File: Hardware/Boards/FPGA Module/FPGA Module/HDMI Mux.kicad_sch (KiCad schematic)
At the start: 3 parts, among them U14 TS3USB221A

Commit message: FPGA Module sch update
Added 3V3 LDO for MCU and 3V3 EN for DCDC. Also added SPI bus from MCU to FPGA with level shifter
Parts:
- added R129: 4.7K, Resistor_SMD:R_0402_1005Metric, symbol Device:R_US
- added TP45: Test Point, FPGA Module:Test Point 0.75mm, symbol Connector:TestPoint
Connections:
- net GND: now also R129.1; no longer U14.6 (~{EN})
- net HDMI_CLK_SEL: now also TP45.1
- new net: R129.2, U14.6 (~{EN})
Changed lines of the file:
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@@
 		(color 0 0 0 0)
 	)
+	(junction
+		(at 179.07 152.4)
+		(diameter 0)
+		(color 0 0 0 0)
+	)
 	(wire
 		(pts
@@
 	(wire
 		(pts
+			(xy 198.12 166.37) (xy 198.12 167.64)
+		)
+		(stroke
+			(width 0)
+			(type default)
+		)
+	)
+	(wire
+		(pts
 			(xy 218.44 128.27) (xy 218.44 129.54)
 		)
@@
 	(wire
 		(pts
+			(xy 179.07 152.4) (xy 185.42 152.4)
+		)
+		(stroke
+			(width 0)
+			(type default)
+		)
+	)
+	(wire
+		(pts
 			(xy 185.42 152.4) (xy 199.39 152.4)
 		)
@@
 	(wire
 		(pts
-			(xy 181.61 152.4) (xy 185.42 152.4)
-		)
-		(stroke
-			(width 0)
-			(type default)
-		)
-	)
-	(wire
-		(pts
-			(xy 198.12 154.94) (xy 198.12 162.56)
+			(xy 175.26 152.4) (xy 179.07 152.4)
+		)
+		(stroke
+			(width 0)
+			(type default)
+		)
+	)
+	(wire
+		(pts
+			(xy 198.12 154.94) (xy 198.12 158.75)
 		)
 		(stroke
@@
 	(hierarchical_label "HDMI_CLK_SEL"
 		(shape input)
-		(at 181.61 152.4 180)
+		(at 175.26 152.4 180)
 		(fields_autoplaced yes)
 		(effects
@@
 	)
 	(symbol
+		(lib_id "Device:R_US")
+		(at 198.12 162.56 180)
+		(unit 1)
+		(exclude_from_sim no)
+		(in_bom yes)
+		(on_board yes)
+		(dnp no)
+		(property "Reference" "R129"
+			(at 200.66 161.2899 0)
+			(effects
+				(font
+					(size 1.27 1.27)
+				)
+				(justify right)
+			)
+		)
+		(property "Value" "4.7K"
+			(at 200.66 163.8299 0)
+			(effects
+				(font
+					(size 1.27 1.27)
+				)
+				(justify right)
+			)
+		)
+		(property "Footprint" "Resistor_SMD:R_0402_1005Metric"
+			(at 197.104 162.306 90)
+			(effects
+				(font
+					(size 1.27 1.27)
+				)
+				(hide yes)
+			)
+		)
+		(property "Datasheet" "~"
+			(at 198.12 162.56 0)
+			(effects
+				(font
+					(size 1.27 1.27)
+				)
+				(hide yes)
+			)
+		)
+		(property "Description" "Resistor, US symbol"
+			(at 198.12 162.56 0)
+			(effects
+				(font
+					(size 1.27 1.27)
+				)
+				(hide yes)
+			)
+		)
+		(pin "1"
+		)
+		(pin "2"
+		)
+		(instances
+			(project "FPGA Module"
+				(path "/199f10e2-d4b4-4a27-9e84-7b1ce2ae6bf0/0c296310-f788-47f0-8a3f-43c3444563e8/e6896036-c481-4794-bc56-64749c97c534"
+					(reference "R129")
+					(unit 1)
+				)
+			)
+		)
+	)
+	(symbol
 		(lib_id "FPGA Module:TS3USB221A")
 		(at 214.63 129.54 0)
@@
 	(symbol
 		(lib_id "power:GND")
-		(at 198.12 162.56 0)
-		(unit 1)
-		(exclude_from_sim no)
-		(in_bom yes)
-		(on_board yes)
-		(dnp no)
-		(property "Reference" "#PWR0268"
-			(at 198.12 168.91 0)
-			(effects
-				(font
-					(size 1.27 1.27)
-				)
-				(hide yes)
-			)
-		)
-		(property "Value" "GND"
-			(at 198.12 166.37 0)
-			(effects
-				(font
-					(size 1.27 1.27)
-				)
-			)
-		)
-		(property "Footprint" ""
-			(at 198.12 162.56 0)
-			(effects
-				(font
-					(size 1.27 1.27)
-				)
-				(hide yes)
-			)
-		)
-		(property "Datasheet" ""
-			(at 198.12 162.56 0)
-			(effects
-				(font
-					(size 1.27 1.27)
-				)
-				(hide yes)
-			)
-		)
-		(property "Description" "Power symbol creates a global label with name \"GND\" , ground"
-			(at 198.12 162.56 0)
-			(effects
-				(font
-					(size 1.27 1.27)
-				)
-				(hide yes)
-			)
-		)
-		(pin "1"
-		)
-		(instances
-			(project "FPGA Module"
-				(path "/199f10e2-d4b4-4a27-9e84-7b1ce2ae6bf0/0c296310-f788-47f0-8a3f-43c3444563e8/e6896036-c481-4794-bc56-64749c97c534"
-					(reference "#PWR0268")
-					(unit 1)
-				)
-			)
-		)
-	)
-	(symbol
-		(lib_id "power:GND")
 		(at 218.44 134.62 0)
 		(unit 1)
@@
 					(unit 1)
 				)
+			)
+		)
+	)
+	(symbol
+		(lib_id "Connector:TestPoint")
+		(at 179.07 152.4 0)
+		(unit 1)
+		(exclude_from_sim no)
+		(in_bom yes)
+		(on_board yes)
+		(dnp no)
+		(property "Reference" "TP45"
+			(at 176.53 147.32 0)
+			(effects
+				(font
+					(size 1.27 1.27)
+				)
+				(justify left)
+			)
+		)
+		(property "Value" "Test Point"
+			(at 173.99 146.685 0)
+			(effects
+				(font
+					(size 1.27 1.27)
+				)
+				(justify left)
+				(hide yes)
+			)
+		)
+		(property "Footprint" "FPGA Module:Test Point 0.75mm"
+			(at 184.15 152.4 0)
+			(effects
+				(font
+					(size 1.27 1.27)
+				)
+				(hide yes)
+			)
+		)
+		(property "Datasheet" "~"
+			(at 184.15 152.4 0)
+			(effects
+				(font
+					(size 1.27 1.27)
+				)
+				(hide yes)
+			)
+		)
+		(property "Description" "test point"
+			(at 179.07 152.4 0)
+			(effects
+				(font
+					(size 1.27 1.27)
+				)
+				(hide yes)
+			)
+		)
+		(pin "1"
+		)
+		(instances
+			(project "FPGA Module"
+				(path "/199f10e2-d4b4-4a27-9e84-7b1ce2ae6bf0/0c296310-f788-47f0-8a3f-43c3444563e8/e6896036-c481-4794-bc56-64749c97c534"
+					(reference "TP45")
+					(unit 1)
+				)
+			)
+		)
+	)
+	(symbol
+		(lib_id "power:GND")
+		(at 198.12 167.64 0)
+		(unit 1)
+		(exclude_from_sim no)
+		(in_bom yes)
+		(on_board yes)
+		(dnp no)
+		(property "Reference" "#PWR0268"
+			(at 198.12 173.99 0)
+			(effects
+				(font
+					(size 1.27 1.27)
+				)
+				(hide yes)
+			)
+		)
+		(property "Value" "GND"
+			(at 198.12 171.45 0)
+			(effects
+				(font
+					(size 1.27 1.27)
+				)
+			)
+		)
+		(property "Footprint" ""
+			(at 198.12 167.64 0)
+			(effects
+				(font
+					(size 1.27 1.27)
+				)
+				(hide yes)
+			)
+		)
+		(property "Datasheet" ""
+			(at 198.12 167.64 0)
+			(effects
+				(font
+					(size 1.27 1.27)
+				)
+				(hide yes)
+			)
+		)
+		(property "Description" "Power symbol creates a global label with name \"GND\" , ground"
+			(at 198.12 167.64 0)
+			(effects
+				(font
+					(size 1.27 1.27)
+				)
+				(hide yes)
+			)
+		)
+		(pin "1"
+		)
+		(instances
+			(project "FPGA Module"
+				(path "/199f10e2-d4b4-4a27-9e84-7b1ce2ae6bf0/0c296310-f788-47f0-8a3f-43c3444563e8/e6896036-c481-4794-bc56-64749c97c534"
+					(reference "#PWR0268")
+					(unit 1)
+				)

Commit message: Completed FPGA module PCB layout
Started PCB routing
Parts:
- C125: renamed from C136; footprint Capacitor_SMD:C_0402_1005Metric -> Capacitor_SMD:C_0201_0603Metric
- R127: renamed from R109; footprint Resistor_SMD:R_0402_1005Metric -> Resistor_SMD:R_0201_0603Metric
- R128: renamed from R129; footprint Resistor_SMD:R_0402_1005Metric -> Resistor_SMD:R_0201_0603Metric
- renumbered TP45 to TP52, U14 to U22
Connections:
- net HDMI_GTCLK_N: now also U22.2 (D1-); no longer U22.4 (D2-)
- net HDMI_GTCLK_P: now also U22.1 (D1+); no longer U22.3 (D2+)
- net HDMI_LVCLK_N: now also U22.4 (D2-); no longer U22.2 (D1-)
- net HDMI_LVCLK_P: now also U22.3 (D2+); no longer U22.1 (D1+)
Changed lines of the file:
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@@
+	(wire
+		(pts
+			(xy 175.26 144.78) (xy 199.39 144.78)
+		)
+		(stroke
+			(width 0)
+			(type default)
+		)
+	)
 	(wire
 		(pts
@@
 	(wire
 		(pts
+			(xy 175.26 129.54) (xy 199.39 129.54)
+		)
+		(stroke
+			(width 0)
+			(type default)
+		)
+	)
+	(wire
+		(pts
 			(xy 198.12 166.37) (xy 198.12 167.64)
 		)
@@
 	(wire
 		(pts
+			(xy 175.26 142.24) (xy 199.39 142.24)
+		)
+		(stroke
+			(width 0)
+			(type default)
+		)
+	)
+	(wire
+		(pts
 			(xy 218.44 128.27) (xy 218.44 129.54)
 		)
@@
 	(wire
 		(pts
-			(xy 175.26 129.54) (xy 199.39 129.54)
-		)
-		(stroke
-			(width 0)
-			(type default)
-		)
-	)
-	(wire
-		(pts
 			(xy 217.17 144.78) (xy 233.68 144.78)
 		)
@@
 	(wire
 		(pts
-			(xy 175.26 142.24) (xy 199.39 142.24)
-		)
-		(stroke
-			(width 0)
-			(type default)
-		)
-	)
-	(wire
-		(pts
-			(xy 175.26 144.78) (xy 199.39 144.78)
-		)
-		(stroke
-			(width 0)
-			(type default)
-		)
-	)
-	(wire
-		(pts
 			(xy 175.26 152.4) (xy 179.07 152.4)
 		)
@@
 		)
 	)
-	(text_box "NOTE: Default is Output ON, HDMI_CLK <- LVDS IO\nPull Sel HIGH to connect HDMI_CLK to MGT IO"
+	(text_box "NOTE: Default is Output ON, HDMI_CLK <- MGT IO\nPull Sel HIGH to connect HDMI_CLK to LVDS IO"
 		(exclude_from_sim no)
 		(at 150.495 155.575 0)
@@
 		)
 	)
+	(label "HDMI_GTCLK_P"
+		(at 175.26 129.54 0)
+		(fields_autoplaced yes)
+		(effects
+			(font
+				(size 1.27 1.27)
+			)
+			(justify left bottom)
+		)
+	)
 	(label "HDMI_CLK_SEL"
 		(at 181.61 152.4 0)
@@
 		)
 	)
+	(label "HDMI_GTCLK_N"
+		(at 175.26 132.08 0)
+		(fields_autoplaced yes)
+		(effects
+			(font
+				(size 1.27 1.27)
+			)
+			(justify left bottom)
+		)
+	)
+	(label "HDMI_LVCLK_P"
+		(at 175.26 142.24 0)
+		(fields_autoplaced yes)
+		(effects
+			(font
+				(size 1.27 1.27)
+			)
+			(justify left bottom)
+		)
+	)
 	(label "HDMI_LVCLK_N"
-		(at 175.26 132.08 0)
-		(fields_autoplaced yes)
-		(effects
-			(font
-				(size 1.27 1.27)
-			)
-			(justify left bottom)
-		)
-	)
-	(label "HDMI_GTCLK_P"
-		(at 175.26 142.24 0)
-		(fields_autoplaced yes)
-		(effects
-			(font
-				(size 1.27 1.27)
-			)
-			(justify left bottom)
-		)
-	)
-	(label "HDMI_GTCLK_N"
 		(at 175.26 144.78 0)
 		(fields_autoplaced yes)
@@
 		)
 	)
-	(label "HDMI_LVCLK_P"
-		(at 175.26 129.54 0)
-		(fields_autoplaced yes)
-		(effects
-			(font
-				(size 1.27 1.27)
-			)
-			(justify left bottom)
-		)
-	)
 	(label "HDMI_CLK_N"
 		(at 233.68 144.78 180)
@@
 	(hierarchical_label "HDMI_LVCLK_N"
 		(shape input)
-		(at 175.26 132.08 180)
+		(at 175.26 144.78 180)
 		(fields_autoplaced yes)
 		(effects
@@
 		)
 	)
-	(hierarchical_label "HDMI_GTCLK_P"
+	(hierarchical_label "HDMI_LVCLK_P"
 		(shape input)
 		(at 175.26 142.24 180)
-		(fields_autoplaced yes)
-		(effects
-			(font
-				(size 1.27 1.27)
-			)
-			(justify right)
-		)
-	)
-	(hierarchical_label "HDMI_LVCLK_P"
-		(shape input)
-		(at 175.26 129.54 180)
-		(fields_autoplaced yes)
-		(effects
-			(font
-				(size 1.27 1.27)
-			)
-			(justify right)
-		)
-	)
-	(hierarchical_label "HDMI_GTCLK_N"
-		(shape input)
-		(at 175.26 144.78 180)
 		(fields_autoplaced yes)
 		(effects
@@
 			)
 			(justify left)
+		)
+	)
+	(hierarchical_label "HDMI_GTCLK_P"
+		(shape input)
+		(at 175.26 129.54 180)
+		(fields_autoplaced yes)
+		(effects
+			(font
+				(size 1.27 1.27)
+			)
+			(justify right)
+		)
+	)
+	(hierarchical_label "HDMI_GTCLK_N"
+		(shape input)
+		(at 175.26 132.08 180)
+		(fields_autoplaced yes)
+		(effects
+			(font
+				(size 1.27 1.27)
+			)
+			(justify right)
 		)
 	)
@@
 		(on_board yes)
 		(dnp no)
-		(property "Reference" "R109"
+		(property "Reference" "R127"
 			(at 187.96 156.2099 0)
 			(effects
@@
 			)
 		)
-		(property "Footprint" "Resistor_SMD:R_0402_1005Metric"
+		(property "Footprint" "Resistor_SMD:R_0201_0603Metric"
 			(at 184.404 157.226 90)
 			(effects
@@
 			(project "FPGA Module"
 				(path "/199f10e2-d4b4-4a27-9e84-7b1ce2ae6bf0/0c296310-f788-47f0-8a3f-43c3444563e8/e6896036-c481-4794-bc56-64749c97c534"
-					(reference "R109")
+					(reference "R127")
 					(unit 1)
 				)
@@
 		(on_board yes)
 		(dnp no)
-		(property "Reference" "C136"
+		(property "Reference" "C125"
 			(at 220.98 130.8162 0)
 			(effects
@@
 			)
 		)
-		(property "Footprint" "Capacitor_SMD:C_0402_1005Metric"
+		(property "Footprint" "Capacitor_SMD:C_0201_0603Metric"
 			(at 218.44 132.08 0)
 			(effects
@@
 			(project "FPGA Module"
 				(path "/199f10e2-d4b4-4a27-9e84-7b1ce2ae6bf0/0c296310-f788-47f0-8a3f-43c3444563e8/e6896036-c481-4794-bc56-64749c97c534"
-					(reference "C136")
+					(reference "C125")
 					(unit 1)
 				)
@@
 		(on_board yes)
 		(dnp no)
-		(property "Reference" "#PWR0267"
+		(property "Reference" "#PWR0276"
 			(at 218.44 168.91 0)
 			(effects
@@
 			(project "FPGA Module"
 				(path "/199f10e2-d4b4-4a27-9e84-7b1ce2ae6bf0/0c296310-f788-47f0-8a3f-43c3444563e8/e6896036-c481-4794-bc56-64749c97c534"
-					(reference "#PWR0267")
+					(reference "#PWR0276")
 					(unit 1)
 				)
@@
 		(on_board yes)
 		(dnp no)
-		(property "Reference" "R129"
+		(property "Reference" "R128"
 			(at 200.66 161.2899 0)
 			(effects
@@
 			)
 		)
-		(property "Footprint" "Resistor_SMD:R_0402_1005Metric"
+		(property "Footprint" "Resistor_SMD:R_0201_0603Metric"
 			(at 197.104 162.306 90)
 			(effects
@@
 			(project "FPGA Module"
 				(path "/199f10e2-d4b4-4a27-9e84-7b1ce2ae6bf0/0c296310-f788-47f0-8a3f-43c3444563e8/e6896036-c481-4794-bc56-64749c97c534"
-					(reference "R129")
+					(reference "R128")
 					(unit 1)
 				)
@@
 		(dnp no)
 		(fields_autoplaced yes)
-		(property "Reference" "U14"
+		(property "Reference" "U22"
 			(at 208.28 121.92 0)
 			(effects
@@
 			(project ""
 				(path "/199f10e2-d4b4-4a27-9e84-7b1ce2ae6bf0/0c296310-f788-47f0-8a3f-43c3444563e8/e6896036-c481-4794-bc56-64749c97c534"
-					(reference "U14")
+					(reference "U22")
 					(unit 1)
 				)
@@
 		(on_board yes)
 		(dnp no)
-		(property "Reference" "#PWR0269"
+		(property "Reference" "#PWR0275"
 			(at 185.42 168.91 0)
 			(effects
@@
 			(project "FPGA Module"
 				(path "/199f10e2-d4b4-4a27-9e84-7b1ce2ae6bf0/0c296310-f788-47f0-8a3f-43c3444563e8/e6896036-c481-4794-bc56-64749c97c534"
-					(reference "#PWR0269")
+					(reference "#PWR0275")
 					(unit 1)
 				)
@@
 		(on_board yes)
 		(dnp no)
-		(property "Reference" "#PWR0265"
+		(property "Reference" "#PWR0274"
 			(at 218.44 140.97 0)
 			(effects
@@
 			(project "FPGA Module"
 				(path "/199f10e2-d4b4-4a27-9e84-7b1ce2ae6bf0/0c296310-f788-47f0-8a3f-43c3444563e8/e6896036-c481-4794-bc56-64749c97c534"
-					(reference "#PWR0265")
+					(reference "#PWR0274")
 					(unit 1)
 				)
@@
 		(on_board yes)
 		(dnp no)
-		(property "Reference" "TP45"
+		(property "Reference" "TP52"
 			(at 176.53 147.32 0)
 			(effects
@@
 			(project "FPGA Module"
 				(path "/199f10e2-d4b4-4a27-9e84-7b1ce2ae6bf0/0c296310-f788-47f0-8a3f-43c3444563e8/e6896036-c481-4794-bc56-64749c97c534"
-					(reference "TP45")
+					(reference "TP52")
 					(unit 1)
 				)
@@
 		(on_board yes)
 		(dnp no)
-		(property "Reference" "#PWR0268"
+		(property "Reference" "#PWR0277"
 			(at 198.12 173.99 0)
 			(effects
@@
 			(project "FPGA Module"
 				(path "/199f10e2-d4b4-4a27-9e84-7b1ce2ae6bf0/0c296310-f788-47f0-8a3f-43c3444563e8/e6896036-c481-4794-bc56-64749c97c534"
-					(reference "#PWR0268")
+					(reference "#PWR0277")
 					(unit 1)
 				)
@@
 		(on_board yes)
 		(dnp no)
-		(property "Reference" "#PWR0266"
+		(property "Reference" "#PWR0273"
 			(at 218.44 132.08 0)
 			(effects
@@
 			(project "FPGA Module"
 				(path "/199f10e2-d4b4-4a27-9e84-7b1ce2ae6bf0/0c296310-f788-47f0-8a3f-43c3444563e8/e6896036-c481-4794-bc56-64749c97c534"
-					(reference "#PWR0266")
+					(reference "#PWR0273")
 					(unit 1)
 				)

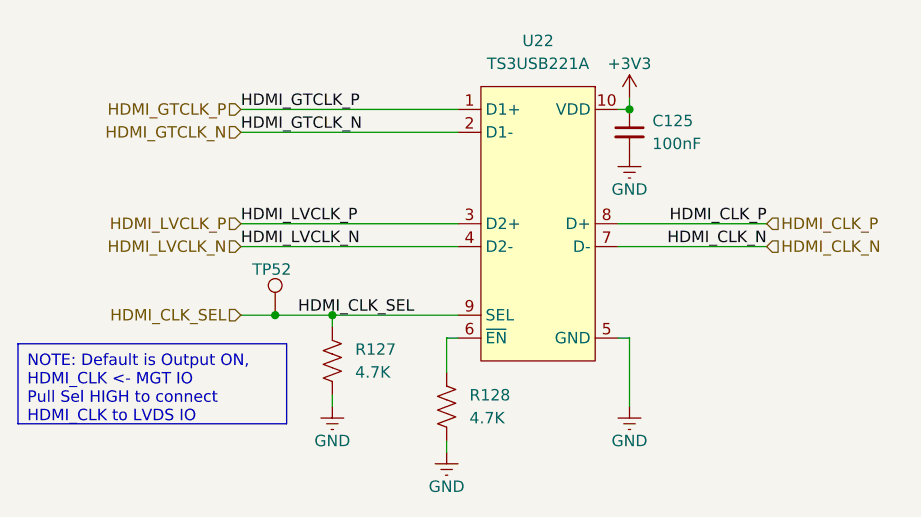
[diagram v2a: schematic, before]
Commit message: Fixed FPGA Module Routing
Reversed B2B headers and re-routed connections to FPGA
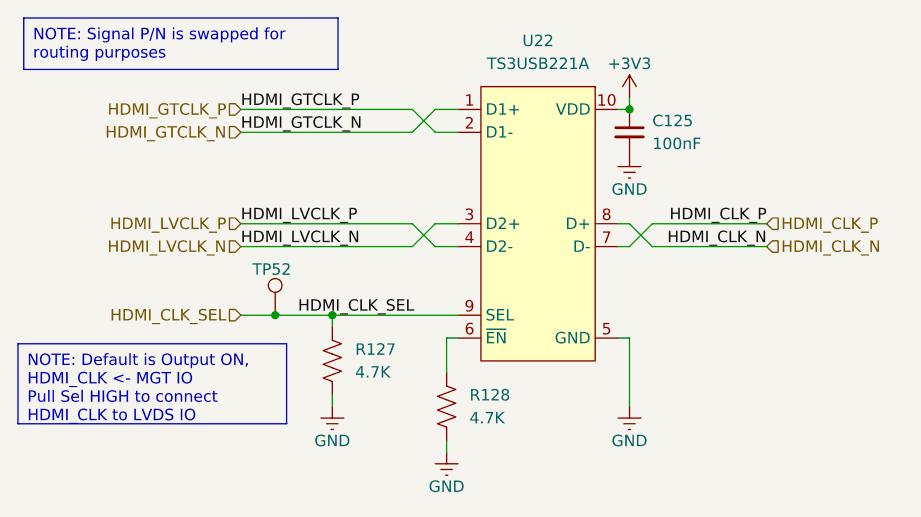
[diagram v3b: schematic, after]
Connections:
- net HDMI_CLK_N: now also U22.8 (D+); no longer U22.7 (D-)
- net HDMI_CLK_P: now also U22.7 (D-); no longer U22.8 (D+)
- net HDMI_GTCLK_N: now also U22.1 (D1+); no longer U22.2 (D1-)
- net HDMI_GTCLK_P: now also U22.2 (D1-); no longer U22.1 (D1+)
- net HDMI_LVCLK_N: now also U22.3 (D2+); no longer U22.4 (D2-)
- net HDMI_LVCLK_P: now also U22.4 (D2-); no longer U22.3 (D2+)
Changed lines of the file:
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@@
 	(wire
 		(pts
-			(xy 175.26 144.78) (xy 199.39 144.78)
+			(xy 217.17 142.24) (xy 218.44 142.24)
+		)
+		(stroke
+			(width 0)
+			(type default)
+		)
+	)
+	(wire
+		(pts
+			(xy 194.31 132.08) (xy 196.85 129.54)
 		)
 		(stroke
@@
 	(wire
 		(pts
-			(xy 175.26 129.54) (xy 199.39 129.54)
-		)
-		(stroke
-			(width 0)
-			(type default)
-		)
-	)
-	(wire
-		(pts
 			(xy 198.12 166.37) (xy 198.12 167.64)
 		)
@@
 	(wire
 		(pts
-			(xy 175.26 142.24) (xy 199.39 142.24)
-		)
-		(stroke
-			(width 0)
-			(type default)
-		)
-	)
-	(wire
-		(pts
 			(xy 218.44 128.27) (xy 218.44 129.54)
 		)
@@
 	(wire
 		(pts
+			(xy 196.85 142.24) (xy 199.39 142.24)
+		)
+		(stroke
+			(width 0)
+			(type default)
+		)
+	)
+	(wire
+		(pts
 			(xy 199.39 154.94) (xy 198.12 154.94)
 		)
@@
 	(wire
 		(pts
+			(xy 194.31 144.78) (xy 196.85 142.24)
+		)
+		(stroke
+			(width 0)
+			(type default)
+		)
+	)
+	(wire
+		(pts
 			(xy 179.07 152.4) (xy 185.42 152.4)
 		)
@@
 	(wire
 		(pts
+			(xy 196.85 144.78) (xy 199.39 144.78)
+		)
+		(stroke
+			(width 0)
+			(type default)
+		)
+	)
+	(wire
+		(pts
+			(xy 220.98 142.24) (xy 218.44 144.78)
+		)
+		(stroke
+			(width 0)
+			(type default)
+		)
+	)
+	(wire
+		(pts
+			(xy 196.85 132.08) (xy 199.39 132.08)
+		)
+		(stroke
+			(width 0)
+			(type default)
+		)
+	)
+	(wire
+		(pts
+			(xy 175.26 129.54) (xy 194.31 129.54)
+		)
+		(stroke
+			(width 0)
+			(type default)
+		)
+	)
+	(wire
+		(pts
 			(xy 185.42 152.4) (xy 199.39 152.4)
 		)
@@
 	(wire
 		(pts
-			(xy 217.17 144.78) (xy 233.68 144.78)
-		)
-		(stroke
-			(width 0)
-			(type default)
-		)
-	)
-	(wire
-		(pts
-			(xy 175.26 132.08) (xy 199.39 132.08)
+			(xy 194.31 142.24) (xy 196.85 144.78)
+		)
+		(stroke
+			(width 0)
+			(type default)
+		)
+	)
+	(wire
+		(pts
+			(xy 175.26 144.78) (xy 194.31 144.78)
+		)
+		(stroke
+			(width 0)
+			(type default)
+		)
+	)
+	(wire
+		(pts
+			(xy 233.68 142.24) (xy 220.98 142.24)
+		)
+		(stroke
+			(width 0)
+			(type default)
+		)
+	)
+	(wire
+		(pts
+			(xy 175.26 142.24) (xy 194.31 142.24)
 		)
 		(stroke
@@
 	(wire
 		(pts
+			(xy 220.98 144.78) (xy 218.44 142.24)
+		)
+		(stroke
+			(width 0)
+			(type default)
+		)
+	)
+	(wire
+		(pts
+			(xy 194.31 129.54) (xy 196.85 132.08)
+		)
+		(stroke
+			(width 0)
+			(type default)
+		)
+	)
+	(wire
+		(pts
 			(xy 185.42 161.29) (xy 185.42 162.56)
 		)
@@
 	(wire
 		(pts
-			(xy 217.17 142.24) (xy 233.68 142.24)
+			(xy 233.68 144.78) (xy 220.98 144.78)
+		)
+		(stroke
+			(width 0)
+			(type default)
+		)
+	)
+	(wire
+		(pts
+			(xy 217.17 144.78) (xy 218.44 144.78)
+		)
+		(stroke
+			(width 0)
+			(type default)
+		)
+	)
+	(wire
+		(pts
+			(xy 196.85 129.54) (xy 199.39 129.54)
 		)
 		(stroke
@@
 		(pts
 			(xy 217.17 129.54) (xy 218.44 129.54)
+		)
+		(stroke
+			(width 0)
+			(type default)
+		)
+	)
+	(wire
+		(pts
+			(xy 175.26 132.08) (xy 194.31 132.08)
 		)
 		(stroke
@@
 		(at 150.495 155.575 0)
 		(size 29.845 8.89)
+		(stroke
+			(width 0)
+			(type default)
+		)
+		(fill
+			(type none)
+		)
+		(effects
+			(font
+				(size 1.27 1.27)
+			)
+			(justify left top)
+		)
+	)
+	(text_box "NOTE: Signal P/N is swapped for routing purposes"
+		(exclude_from_sim no)
+		(at 151.13 119.38 0)
+		(size 34.925 5.715)
 		(stroke
 			(width 0)
@@
 			)
 		)
-		(property "Datasheet" "https://www.ti.com/lit/ds/symlink/tmux121.pdf?ts=1704222518748"
+		(property "Datasheet" "https://www.ti.com/lit/ds/symlink/ts3usb221a.pdf?HQS=dis-dk-null-digikeymode-dsf-pf-null-wwe&ts=1726459795164&ref_url=https%253A%252F%252Fwww.ti.com%252Fgeneral%252Fdocs%252Fsuppproductinfo.tsp%253FdistId%253D10%2526gotoUrl%253Dhttps%253A%252F%252Fwww.ti.com%252Flit%252Fgpn%252Fts3usb221a"
 			(at 208.28 160.02 0)
 			(effects

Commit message: Generated FPGA module gerbers
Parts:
- TP52: footprint FPGA Module:Test Point 0.75mm -> FPGA Module:Test Point 0.5mm No Silk
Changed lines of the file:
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@@
 			)
 		)
-		(property "Footprint" "FPGA Module:Test Point 0.75mm"
+		(property "Footprint" "FPGA Module:Test Point 0.5mm No Silk"
 			(at 184.15 152.4 0)
 			(effects
